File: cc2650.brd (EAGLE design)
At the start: 50.8 x 22.9 mm, 28 parts, among them IC1 TPS73133DBVR, IC4 CC2650MODAMOHR, SW1 SPST_TACT-KMR2, SW3 SPST_TACT-KMR2, U2 Value

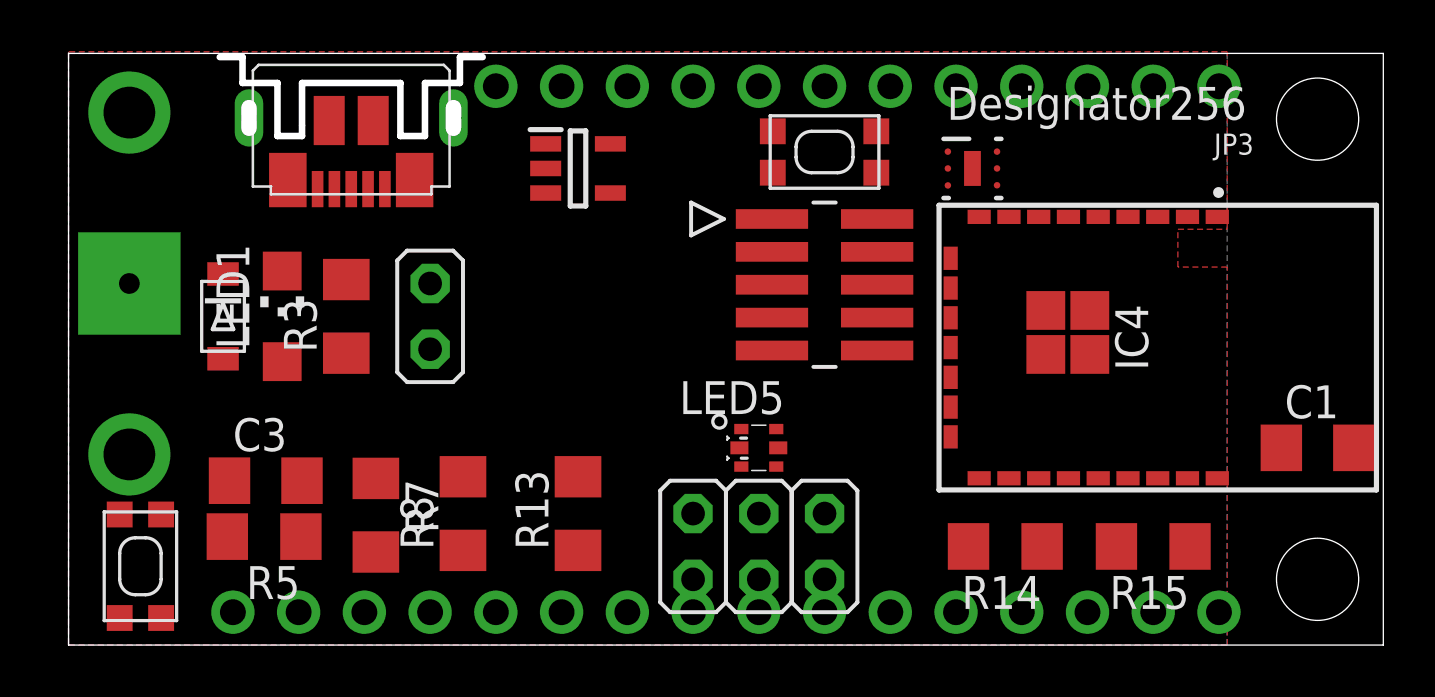
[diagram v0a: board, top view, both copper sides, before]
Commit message: Got rid of text.
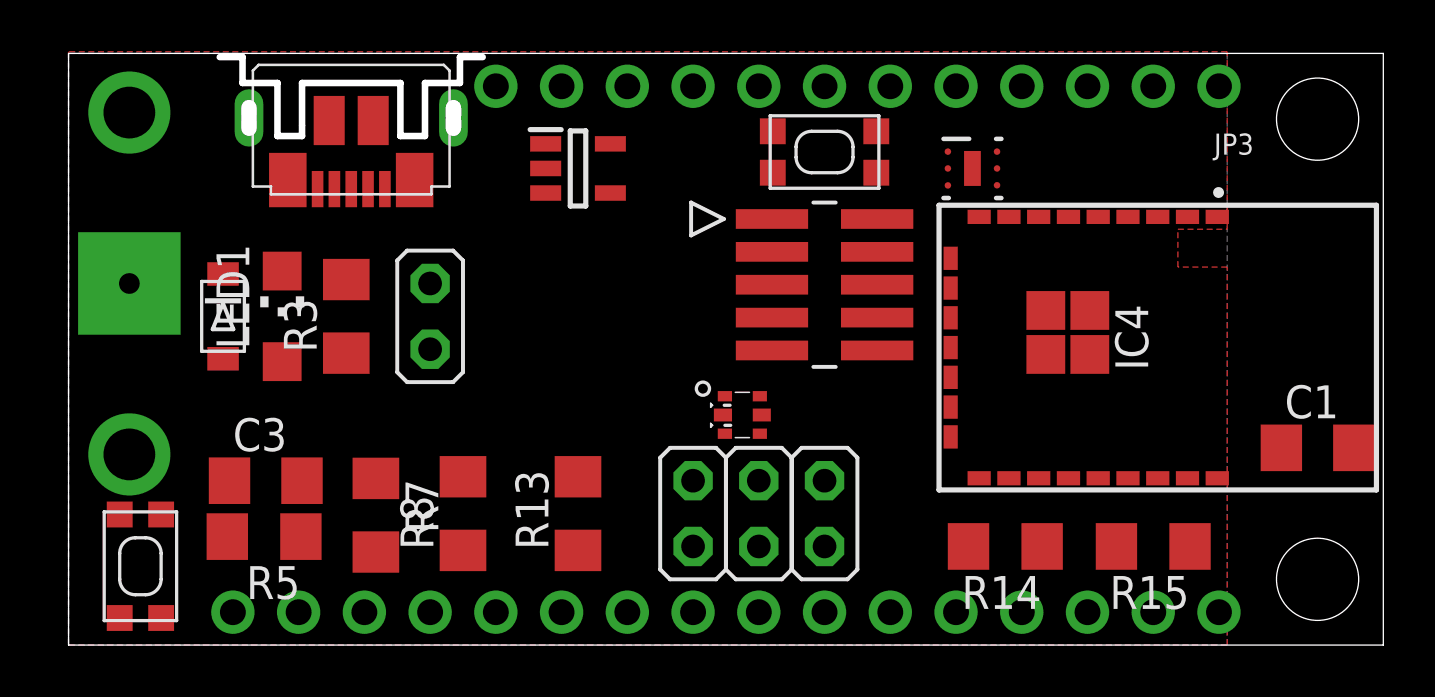
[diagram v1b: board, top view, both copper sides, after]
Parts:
- moved LED5 1.42 mm to (26.0, 8.89)
- moved JP4 1.27 mm to (24.1, 5.08)
- moved JP5 1.27 mm to (26.7, 5.08)
- moved JP6 1.27 mm to (29.2, 5.08)
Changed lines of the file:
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@@
 <attribute name="OC_NEWARK" value="unknown" x="3.175" y="61.595" size="1.778" layer="27" display="off"/>
 </element>
-<element name="JP4" library="jumper" package="JP1M" value="LED2_RED" x="24.13" y="3.81" smashed="yes"/>
-<element name="JP5" library="jumper" package="JP1M" value="LED2_GREEN" x="26.67" y="3.81" smashed="yes"/>
-<element name="JP6" library="jumper" package="JP1M" value="LED2_BLUE" x="29.21" y="3.81" smashed="yes"/>
-<element name="LED5" library="MSP-EXP432" package="RGB_LED" value="EVERLIGHT_19-337" x="26.67" y="7.62"/>
+<element name="JP4" library="jumper" package="JP1M" value="LED2_RED" x="24.13" y="5.08" smashed="yes"/>
+<element name="JP5" library="jumper" package="JP1M" value="LED2_GREEN" x="26.67" y="5.08" smashed="yes"/>
+<element name="JP6" library="jumper" package="JP1M" value="LED2_BLUE" x="29.21" y="5.08" smashed="yes"/>
+<element name="LED5" library="MSP-EXP432" package="RGB_LED" value="EVERLIGHT_19-337" x="26.035" y="8.89" smashed="yes"/>
 <element name="U$6" library="MSP-EXP432" package="MOUNTHOLE_125MIL" value="MOUNTHOLE_125MIL" x="48.26" y="20.32"/>
 <element name="U$7" library="MSP-EXP432" package="MOUNTHOLE_125MIL" value="MOUNTHOLE_125MIL" x="48.26" y="2.54"/>
@@
 <wire x1="20.935" y1="17.465" x2="27.178" y2="15.192" width="0" layer="19" extent="1-1"/>
 <wire x1="18.435" y1="18.415" x2="20.935" y2="17.465" width="0" layer="19" extent="1-1"/>
-<wire x1="25.995" y1="8.345" x2="18.435" y2="18.415" width="0" layer="19" extent="1-1"/>
-<wire x1="25.92" y1="7.62" x2="25.995" y2="8.345" width="0" layer="19" extent="1-1"/>
-<wire x1="25.995" y1="6.895" x2="25.92" y2="7.62" width="0" layer="19" extent="1-1"/>
-<wire x1="12.222" y1="17.617" x2="25.995" y2="8.345" width="0" layer="19" extent="1-1"/>
+<wire x1="25.36" y1="9.615" x2="18.435" y2="18.415" width="0" layer="19" extent="1-1"/>
+<wire x1="25.285" y1="8.89" x2="25.36" y2="9.615" width="0" layer="19" extent="1-1"/>
+<wire x1="25.36" y1="8.165" x2="25.285" y2="8.89" width="0" layer="19" extent="1-1"/>
+<wire x1="12.222" y1="17.617" x2="25.36" y2="9.615" width="0" layer="19" extent="1-1"/>
 <wire x1="8.255" y1="14.45" x2="12.222" y2="17.617" width="0" layer="19" extent="1-1"/>
 <wire x1="2.3495" y1="13.97" x2="8.255" y2="14.45" width="0" layer="19" extent="1-1"/>
@@
 <contactref element="JP4" pad="2"/>
 <contactref element="R15" pad="1"/>
-<wire x1="24.13" y1="5.08" x2="43.332" y2="3.81" width="0" layer="19" extent="1-1"/>
+<wire x1="24.13" y1="6.35" x2="43.332" y2="3.81" width="0" layer="19" extent="1-1"/>
 </signal>
 <signal name="N$4">
 <contactref element="LED5" pad="5"/>
 <contactref element="R15" pad="2"/>
-<wire x1="27.42" y1="7.62" x2="40.488" y2="3.81" width="0" layer="19" extent="1-1"/>
+<wire x1="26.785" y1="8.89" x2="40.488" y2="3.81" width="0" layer="19" extent="1-1"/>
 </signal>
 <signal name="N$5">
 <contactref element="LED5" pad="6"/>
 <contactref element="R14" pad="2"/>
-<wire x1="27.345" y1="6.895" x2="34.773" y2="3.81" width="0" layer="19" extent="1-1"/>
+<wire x1="26.71" y1="8.165" x2="34.773" y2="3.81" width="0" layer="19" extent="1-1"/>
 </signal>
 <signal name="N$6">
 <contactref element="LED5" pad="4"/>
 <contactref element="R13" pad="2"/>
-<wire x1="27.345" y1="8.345" x2="19.685" y2="6.502" width="0" layer="19" extent="1-1"/>
+<wire x1="26.71" y1="9.615" x2="19.685" y2="6.502" width="0" layer="19" extent="1-1"/>
 </signal>
 <signal name="N$7">
 <contactref element="JP5" pad="2"/>
 <contactref element="R14" pad="1"/>
-<wire x1="26.67" y1="5.08" x2="37.617" y2="3.81" width="0" layer="19" extent="1-1"/>
+<wire x1="26.67" y1="6.35" x2="37.617" y2="3.81" width="0" layer="19" extent="1-1"/>
 </signal>
 <signal name="N$12">
 <contactref element="JP6" pad="2"/>
 <contactref element="R13" pad="1"/>
-<wire x1="29.21" y1="5.08" x2="19.685" y2="3.658" width="0" layer="19" extent="1-1"/>
+<wire x1="29.21" y1="6.35" x2="19.685" y2="3.658" width="0" layer="19" extent="1-1"/>
 </signal>
 <signal name="N$9">

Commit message: moved some components to bottom side of the board.
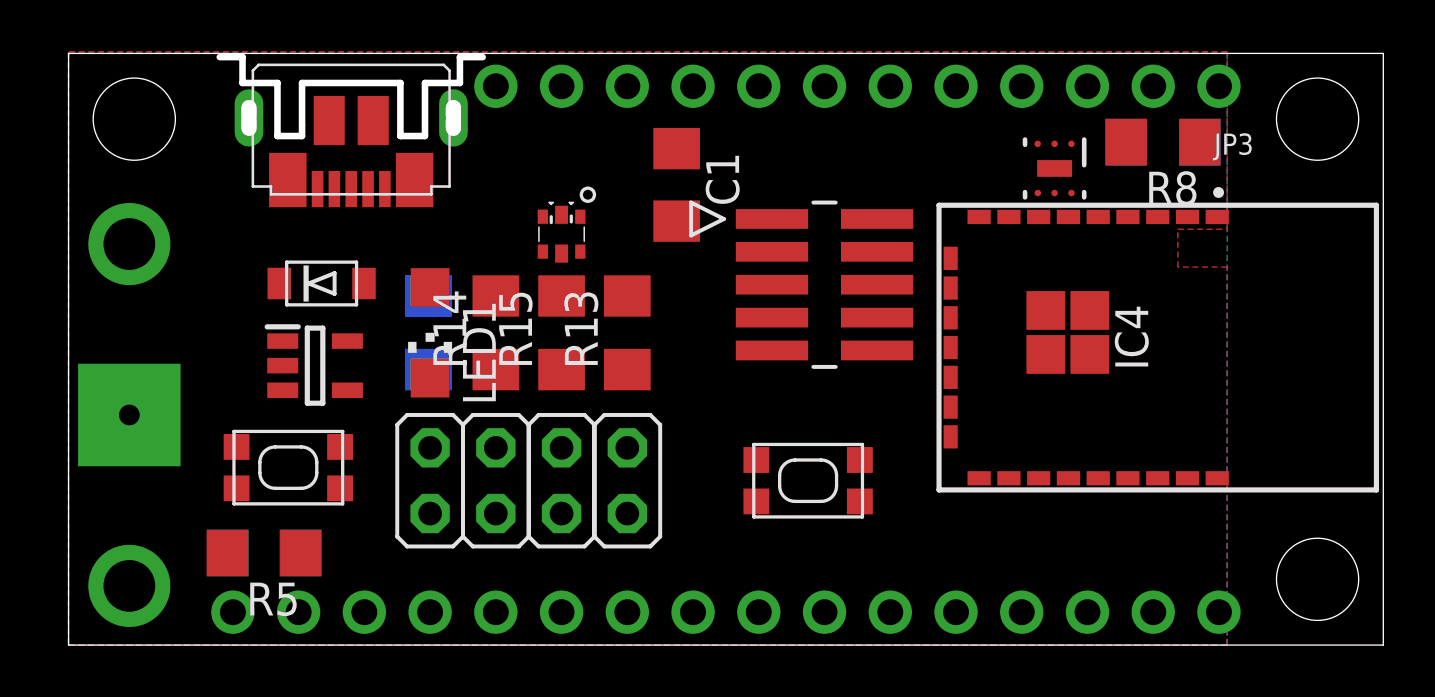
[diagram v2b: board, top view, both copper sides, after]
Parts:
- added U$2: MOUNTHOLE_125MIL, MSP-EXP432:MOUNTHOLE_125MIL
- moved R7 33.7 mm to (42.3, 19.4), flipped to the bottom, turned to 0 degrees
- moved R8 30.6 mm to (42.3, 19.4), turned to 180 degrees
- moved C1 26.8 mm to (23.5, 17.8), turned to 270 degrees
- moved R15 24.3 mm to (19.1, 12.1), turned to 90 degrees
- moved R14 21.3 mm to (16.5, 12.1), turned to 90 degrees
- moved SW3 12.7 mm to (28.6, 6.35)
- moved IC1 12.7 mm to (9.53, 10.8)
- moved JP5 10.2 mm to (16.5, 6.35)
- moved LED5 9.88 mm to (19.1, 15.9), turned to 270 degrees
- moved JP6 7.73 mm to (21.6, 6.35)
- moved R13 7.24 mm to (21.6, 12.1)
- moved SW1 6.87 mm to (8.49, 6.86), turned to 0 degrees
- moved JP1 6.35 mm to (14.0, 6.35)
- moved LED1 5.75 mm to (14.0, 12.1), turned to 180 degrees
- moved JP4 5.24 mm to (19.1, 6.35)
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
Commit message: changed btn pin from DIO4 -> DIO14. Rotated/moved res.
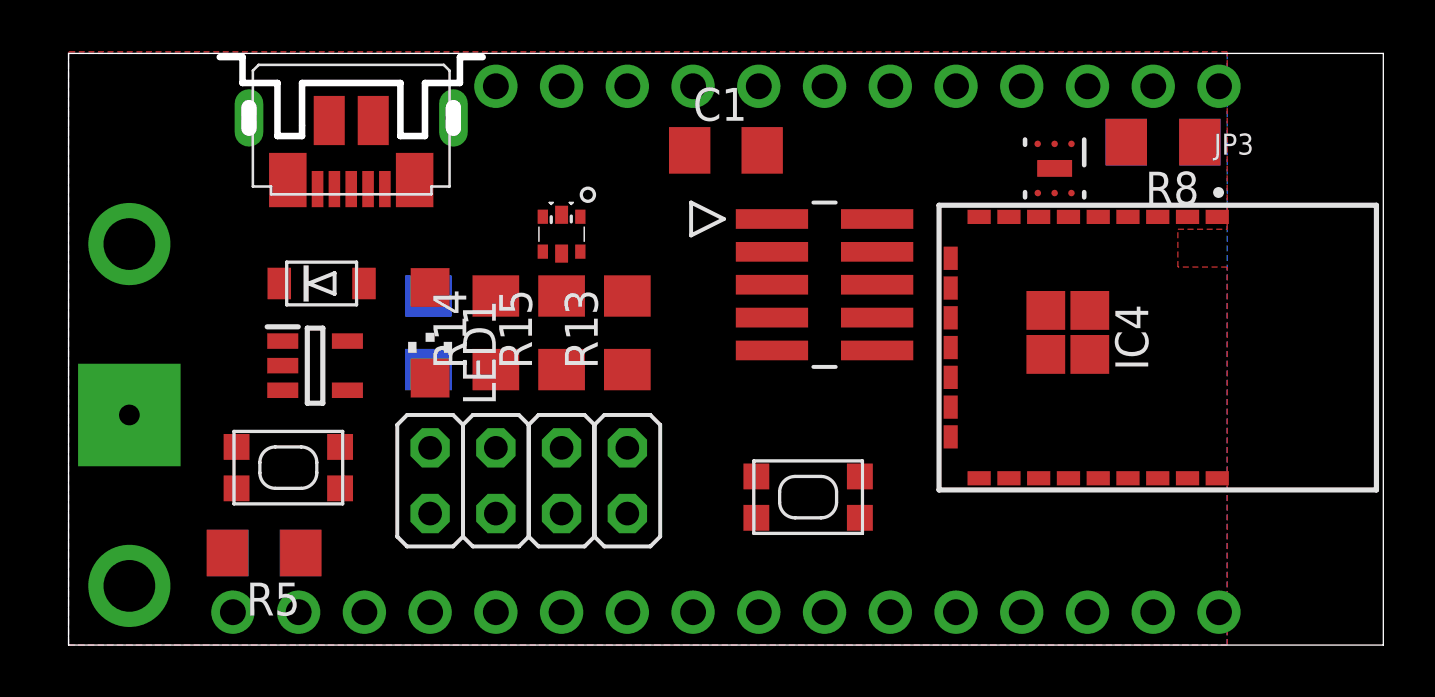
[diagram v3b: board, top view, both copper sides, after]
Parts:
- removed U$2, U$6, U$7: MOUNTHOLE_125MIL, MSP-EXP432:MOUNTHOLE_125MIL
- moved C1 2.33 mm to (25.4, 19.1), turned to 0 degrees
- moved SW3 0.63 mm to (28.6, 5.71)
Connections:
- net DIO14: now also SW3.2, SW3.4
- net DIO4: no longer SW3.2, SW3.4
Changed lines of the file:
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@@
 <param name="TopRouterVariant" value="0"/>
 <param name="tpViaShape" value="round"/>
-<param name="PrefDir.1" value="-"/>
+<param name="PrefDir.1" value="a"/>
 <param name="PrefDir.2" value="0"/>
 <param name="PrefDir.3" value="0"/>
@@
 <param name="PrefDir.14" value="0"/>
 <param name="PrefDir.15" value="0"/>
-<param name="PrefDir.16" value="|"/>
+<param name="PrefDir.16" value="a"/>
 <param name="cfVia" value="8"/>
 <param name="cfNonPref" value="5"/>
@@
 </element>
 <element name="U$1" library="adafruit" package="CR1220-THM" value="" x="2.3495" y="8.89" rot="MR270"/>
-<element name="SW3" library="adafruit" package="KMR2" value="SPST_TACT-KMR2" x="28.575" y="6.35" smashed="yes">
-<attribute name="MF" value="" x="2.54" y="48.895" size="1.778" layer="27" display="off"/>
-<attribute name="MPN" value="" x="2.54" y="48.895" size="1.778" layer="27" display="off"/>
-<attribute name="OC_NEWARK" value="unknown" x="2.54" y="48.895" size="1.778" layer="27" display="off"/>
+<element name="SW3" library="adafruit" package="KMR2" value="SPST_TACT-KMR2" x="28.575" y="5.715" smashed="yes">
+<attribute name="MF" value="" x="2.54" y="48.26" size="1.778" layer="27" display="off"/>
+<attribute name="MPN" value="" x="2.54" y="48.26" size="1.778" layer="27" display="off"/>
+<attribute name="OC_NEWARK" value="unknown" x="2.54" y="48.26" size="1.778" layer="27" display="off"/>
 </element>
 <element name="JP4" library="jumper" package="JP1M" value="LED2_RED" x="19.05" y="6.35" smashed="yes"/>
@@
 <element name="JP6" library="jumper" package="JP1M" value="LED2_BLUE" x="21.59" y="6.35" smashed="yes"/>
 <element name="LED5" library="MSP-EXP432" package="RGB_LED" value="EVERLIGHT_19-337" x="19.05" y="15.875" smashed="yes" rot="R270"/>
-<element name="U$6" library="MSP-EXP432" package="MOUNTHOLE_125MIL" value="MOUNTHOLE_125MIL" x="48.26" y="20.32"/>
-<element name="U$7" library="MSP-EXP432" package="MOUNTHOLE_125MIL" value="MOUNTHOLE_125MIL" x="48.26" y="2.54"/>
 <element name="U2" library="OPT3001" package="DNP0006A" value="Value" x="38.1" y="18.415" smashed="yes" rot="R270">
 <attribute name="APPLICATION_BUILDNUMBER" value="*" x="38.1" y="18.415" size="1.778" layer="27" rot="R270" display="off"/>
@@
 <element name="R14" library="adafruit" package="R1206" value="16" x="16.51" y="12.065" rot="R90"/>
 <element name="R15" library="adafruit" package="R1206" value="110" x="19.05" y="12.065" rot="R90"/>
-<element name="C1" library="adafruit" package="C1206" value="100n" x="23.495" y="17.78" rot="R270"/>
+<element name="C1" library="adafruit" package="C1206" value="100n" x="25.4" y="19.1135"/>
 <element name="C3" library="adafruit" package="C1206" value="1n" x="7.5565" y="3.556" rot="MR0"/>
 <element name="LED1" library="adafruit" package="CHIPLED_1206" value="RED" x="13.97" y="12.065" rot="R180"/>
@@
 <attribute name="VALUE" x="12.7" y="2.032" size="1.27" layer="27" ratio="10"/>
 </element>
-<element name="U$2" library="MSP-EXP432" package="MOUNTHOLE_125MIL" value="MOUNTHOLE_125MIL" x="2.54" y="20.32"/>
 </elements>
 <signals>
@@
 <wire x1="29.21" y1="21.59" x2="37.445" y2="19.365" width="0" layer="19" extent="1-1"/>
 <wire x1="26.67" y1="21.59" x2="29.21" y2="21.59" width="0" layer="19" extent="1-1"/>
-<wire x1="23.495" y1="16.38" x2="26.67" y2="21.59" width="0" layer="19" extent="1-1"/>
-<wire x1="19.775" y1="16.55" x2="23.495" y2="16.38" width="0" layer="19" extent="1-1"/>
+<wire x1="26.8" y1="19.1135" x2="26.67" y2="21.59" width="0" layer="19" extent="1-1"/>
+<wire x1="19.775" y1="16.55" x2="26.8" y2="19.1135" width="0" layer="19" extent="1-1"/>
 <wire x1="19.05" y1="16.625" x2="19.775" y2="16.55" width="0" layer="19" extent="1-1"/>
 <wire x1="18.325" y1="16.55" x2="19.05" y2="16.625" width="0" layer="19" extent="1-1"/>
-<wire x1="27.178" y1="15.192" x2="23.495" y2="16.38" width="0" layer="19" extent="1-1"/>
+<wire x1="27.178" y1="15.192" x2="26.8" y2="19.1135" width="0" layer="19" extent="1-1"/>
 <wire x1="27.178" y1="13.922" x2="27.178" y2="15.192" width="0" layer="19" extent="1-1"/>
 <wire x1="27.178" y1="11.382" x2="27.178" y2="13.922" width="0" layer="19" extent="1-1"/>
-<wire x1="26.575" y1="7.15" x2="27.178" y2="11.382" width="0" layer="19" extent="1-1"/>
-<wire x1="30.575" y1="7.15" x2="26.575" y2="7.15" width="0" layer="19" extent="1-1"/>
-<wire x1="13.97" y1="10.315" x2="18.325" y2="16.55" width="0" layer="19" extent="1-1"/>
-<wire x1="12.222" y1="17.617" x2="13.97" y2="10.315" width="0" layer="19" extent="1-1"/>
+<wire x1="26.575" y1="6.515" x2="27.178" y2="11.382" width="0" layer="19" extent="1-1"/>
+<wire x1="30.575" y1="6.515" x2="26.575" y2="6.515" width="0" layer="19" extent="1-1"/>
+<wire x1="12.222" y1="17.617" x2="18.325" y2="16.55" width="0" layer="19" extent="1-1"/>
+<wire x1="13.97" y1="10.315" x2="12.222" y2="17.617" width="0" layer="19" extent="1-1"/>
 <wire x1="10.775" y1="9.845" x2="13.97" y2="10.315" width="0" layer="19" extent="1-1"/>
 <wire x1="10.492" y1="7.655" x2="10.775" y2="9.845" width="0" layer="19" extent="1-1"/>
@@
 <contactref element="IC4" pad="8"/>
 <contactref element="JP3" pad="3"/>
-<contactref element="SW3" pad="2"/>
-<contactref element="SW3" pad="4"/>
 <wire x1="36.334" y1="16.5435" x2="39.37" y2="21.59" width="0" layer="19" extent="1-1"/>
-<wire x1="30.575" y1="5.55" x2="36.334" y2="16.5435" width="0" layer="19" extent="1-1"/>
-<wire x1="26.575" y1="5.55" x2="30.575" y2="5.55" width="0" layer="19" extent="1-1"/>
 </signal>
 <signal name="N$32">
@@
 <contactref element="IC4" pad="21"/>
 <contactref element="JP2" pad="9"/>
-<wire x1="26.67" y1="1.27" x2="39.784" y2="6.4435" width="0" layer="19" extent="1-1"/>
+<contactref element="SW3" pad="2"/>
+<contactref element="SW3" pad="4"/>
+<wire x1="30.575" y1="4.915" x2="39.784" y2="6.4435" width="0" layer="19" extent="1-1"/>
+<wire x1="26.575" y1="4.915" x2="30.575" y2="4.915" width="0" layer="19" extent="1-1"/>
+<wire x1="26.67" y1="1.27" x2="26.575" y2="4.915" width="0" layer="19" extent="1-1"/>
 </signal>
 <signal name="DIO13">
@@
 <wire x1="38.1" y1="19.365" x2="38.75" y2="19.365" width="0" layer="19" extent="1-1"/>
 <wire x1="27.178" y1="16.462" x2="38.1" y2="19.365" width="0" layer="19" extent="1-1"/>
-<wire x1="23.495" y1="19.18" x2="27.178" y2="16.462" width="0" layer="19" extent="1-1"/>
-<wire x1="24.13" y1="21.59" x2="23.495" y2="19.18" width="0" layer="19" extent="1-1"/>
+<wire x1="24" y1="19.1135" x2="27.178" y2="16.462" width="0" layer="19" extent="1-1"/>
+<wire x1="24.13" y1="21.59" x2="24" y2="19.1135" width="0" layer="19" extent="1-1"/>
 <wire x1="40.934" y1="6.4435" x2="40.869" y2="19.431" width="0" layer="19" extent="1-16"/>
 <wire x1="42.084" y1="6.4435" x2="40.934" y2="6.4435" width="0" layer="19" extent="1-1"/>
-<wire x1="10.775" y1="11.745" x2="23.495" y2="19.18" width="0" layer="19" extent="1-1"/>
+<wire x1="10.775" y1="11.745" x2="24" y2="19.1135" width="0" layer="19" extent="1-1"/>
 <wire x1="13.97" y1="5.08" x2="10.775" y2="11.745" width="0" layer="19" extent="1-1"/>
 <wire x1="11.43" y1="1.27" x2="13.97" y2="5.08" width="0" layer="19" extent="1-1"/>
@@
 <contactref element="JP4" pad="2"/>
 <contactref element="R15" pad="1"/>
-<wire x1="19.05" y1="7.62" x2="19.05" y2="10.643" width="0" layer="19" extent="16-16"/>
+<wire x1="19.05" y1="7.62" x2="19.05" y2="10.643" width="0" layer="19" extent="1-1"/>
 </signal>
 <signal name="N$4">
 <contactref element="LED5" pad="5"/>
 <contactref element="R15" pad="2"/>
-<wire x1="19.05" y1="13.487" x2="19.05" y2="15.125" width="0" layer="19" extent="1-16"/>
+<wire x1="19.05" y1="13.487" x2="19.05" y2="15.125" width="0" layer="19" extent="1-1"/>
 </signal>
 <signal name="N$5">
 <contactref element="LED5" pad="6"/>
 <contactref element="R14" pad="2"/>
-<wire x1="16.51" y1="13.487" x2="18.325" y2="15.2" width="0" layer="19" extent="1-16"/>
+<wire x1="16.51" y1="13.487" x2="18.325" y2="15.2" width="0" layer="19" extent="1-1"/>
 </signal>
 <signal name="N$6">
 <contactref element="LED5" pad="4"/>
 <contactref element="R13" pad="2"/>
-<wire x1="19.775" y1="15.2" x2="21.59" y2="13.487" width="0" layer="19" extent="1-16"/>
+<wire x1="19.775" y1="15.2" x2="21.59" y2="13.487" width="0" layer="19" extent="1-1"/>
 </signal>
 <signal name="N$7">
 <contactref element="JP5" pad="2"/>
 <contactref element="R14" pad="1"/>
-<wire x1="16.51" y1="7.62" x2="16.51" y2="10.643" width="0" layer="19" extent="16-16"/>
+<wire x1="16.51" y1="7.62" x2="16.51" y2="10.643" width="0" layer="19" extent="1-1"/>
 </signal>
 <signal name="N$12">
 <contactref element="JP6" pad="2"/>
 <contactref element="R13" pad="1"/>
-<wire x1="21.59" y1="7.62" x2="21.59" y2="10.643" width="0" layer="19" extent="16-16"/>
+<wire x1="21.59" y1="7.62" x2="21.59" y2="10.643" width="0" layer="19" extent="1-1"/>
 </signal>
 <signal name="N$9">

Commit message: completed BOM through eagle. RGB led not in eagle choices. 12 & 16 pin headers chosen as signle adafruit feather pin kit.
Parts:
- renumbered U2 to OPT3001
